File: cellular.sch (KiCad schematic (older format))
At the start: 16 parts

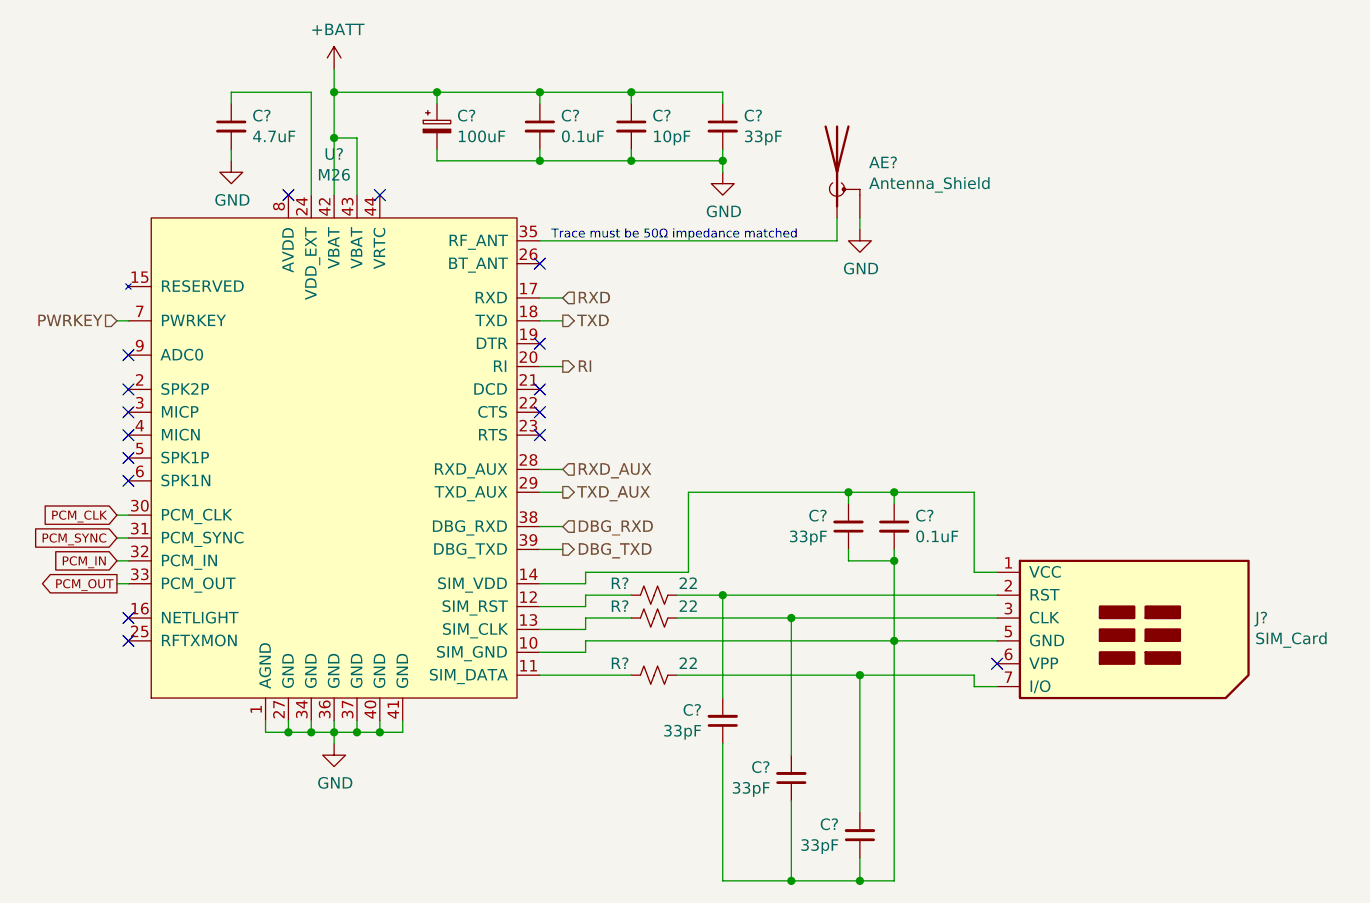
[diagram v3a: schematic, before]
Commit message: annotate schematic and tweak some footprint associations
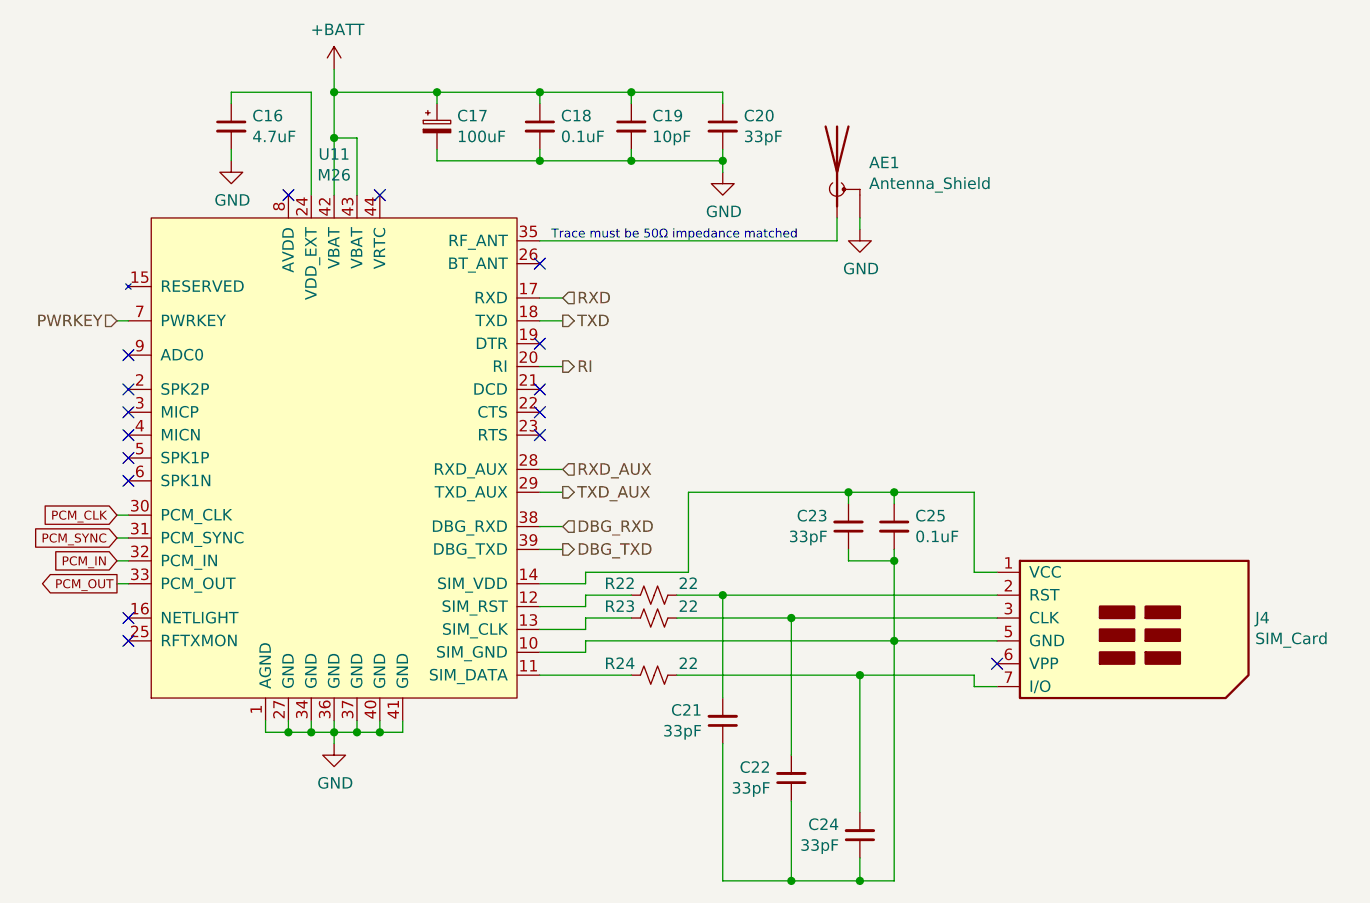
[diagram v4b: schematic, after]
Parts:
- gave numbers to parts that had none: 16
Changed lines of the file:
@@
 $EndDescr
 $Comp
-L phone:M26 U?
+L phone:M26 U11
 U 1 1 5C9AECA6
 P 2250 2550
-F 0 "U?" H 2250 3878 50  0000 C CNN
+F 0 "U11" H 2250 3878 50  0000 C CNN
 F 1 "M26" H 2250 3787 50  0000 C CNN
 F 2 "phone:M26" H 2250 2550 50  0001 C CNN
@@
 NoConn ~ 1350 2650
 $Comp
-L Device:Antenna_Shield AE?
+L Device:Antenna_Shield AE1
 U 1 1 5C9AEE16
 P 4450 1300
-F 0 "AE?" H 4590 1341 50  0000 L CNN
+F 0 "AE1" H 4590 1341 50  0000 L CNN
 F 1 "Antenna_Shield" H 4590 1250 50  0000 L CNN
 F 2 "Connector_Coaxial:U.FL_Molex_MCRF_73412-0110_Vertical" H 4450 1400 50  0001 C CNN
@@
 	4450 1600 4450 1500
 $Comp
-L power:GND #PWR?
+L power:GND #PWR058
 U 1 1 5C9AEED4
 P 4550 1550
-F 0 "#PWR?" H 4550 1300 50  0001 C CNN
+F 0 "#PWR058" H 4550 1300 50  0001 C CNN
 F 1 "GND" H 4555 1377 50  0000 C CNN
 F 2 "" H 4550 1550 50  0001 C CNN
@@
 NoConn ~ 1350 3250
 $Comp
-L power:GND #PWR?
+L power:GND #PWR056
 U 1 1 5C9B042C
 P 2250 3800
-F 0 "#PWR?" H 2250 3550 50  0001 C CNN
+F 0 "#PWR056" H 2250 3550 50  0001 C CNN
 F 1 "GND" H 2255 3627 50  0000 C CNN
 F 2 "" H 2250 3800 50  0001 C CNN
@@
 	2250 3750 2250 3800
 $Comp
-L Connector:SIM_Card J?
+L Connector:SIM_Card J4
 U 1 1 5C9B0C92
 P 5650 3350
-F 0 "J?" H 6279 3450 50  0000 L CNN
+F 0 "J4" H 6279 3450 50  0000 L CNN
 F 1 "SIM_Card" H 6279 3359 50  0000 L CNN
 F 2 "phone:7112S0815X19LF" H 5650 3700 50  0001 C CNN
@@
 	2350 1150 2250 1150
 $Comp
-L power:+BATT #PWR?
+L power:+BATT #PWR055
 U 1 1 5CA67C60
 P 2250 850
-F 0 "#PWR?" H 2250 700 50  0001 C CNN
+F 0 "#PWR055" H 2250 700 50  0001 C CNN
 F 1 "+BATT" H 2265 1023 50  0000 C CNN
 F 2 "" H 2250 850 50  0001 C CNN
@@
 NoConn ~ 2050 1400
 $Comp
-L Device:C_Small C?
+L Device:C_Small C16
 U 1 1 5D5D7303
 P 1800 1100
-F 0 "C?" H 1892 1146 50  0000 L CNN
+F 0 "C16" H 1892 1146 50  0000 L CNN
 F 1 "4.7uF" H 1892 1055 50  0000 L CNN
 F 2 "Capacitor_SMD:C_0603_1608Metric_Pad1.05x0.95mm_HandSolder" H 1800 1100 50  0001 C CNN
@@
 $EndComp
 $Comp
-L power:GND #PWR?
+L power:GND #PWR054
 U 1 1 5D5D9D65
 P 1800 1250
-F 0 "#PWR?" H 1800 1000 50  0001 C CNN
+F 0 "#PWR054" H 1800 1000 50  0001 C CNN
 F 1 "GND" H 1805 1077 50  0000 C CNN
 F 2 "" H 1800 1250 50  0001 C CNN
@@
 	1800 950  1800 1000
 $Comp
-L Device:C_Small C?
+L Device:C_Small C25
 U 1 1 5D5DD206
 P 4700 2850
-F 0 "C?" H 4792 2896 50  0000 L CNN
+F 0 "C25" H 4792 2896 50  0000 L CNN
 F 1 "0.1uF" H 4792 2805 50  0000 L CNN
 F 2 "Capacitor_SMD:C_0603_1608Metric_Pad1.05x0.95mm_HandSolder" H 4700 2850 50  0001 C CNN
@@
 NoConn ~ 5150 3450
 $Comp
-L Device:R_Small_US R?
+L Device:R_Small_US R22
 U 1 1 5D5E2ECB
 P 3650 3150
-F 0 "R?" V 3600 3000 50  0000 C CNN
+F 0 "R22" V 3600 3000 50  0000 C CNN
 F 1 "22" V 3600 3300 50  0000 C CNN
 F 2 "Resistor_SMD:R_0603_1608Metric_Pad1.05x0.95mm_HandSolder" H 3650 3150 50  0001 C CNN
@@
 	3750 3150 3950 3150
 $Comp
-L Device:R_Small_US R?
+L Device:R_Small_US R23
 U 1 1 5D5E8317
 P 3650 3250
-F 0 "R?" V 3600 3100 50  0000 C CNN
+F 0 "R23" V 3600 3100 50  0000 C CNN
 F 1 "22" V 3600 3400 50  0000 C CNN
 F 2 "Resistor_SMD:R_0603_1608Metric_Pad1.05x0.95mm_HandSolder" H 3650 3250 50  0001 C CNN
@@
 Connection ~ 4700 2700
 $Comp
-L Device:R_Small_US R?
+L Device:R_Small_US R24
 U 1 1 5D5F3F1B
 P 3650 3500
-F 0 "R?" V 3600 3350 50  0000 C CNN
+F 0 "R24" V 3600 3350 50  0000 C CNN
 F 1 "22" V 3600 3650 50  0000 C CNN
 F 2 "Resistor_SMD:R_0603_1608Metric_Pad1.05x0.95mm_HandSolder" H 3650 3500 50  0001 C CNN
@@
 	5050 3500 4550 3500
 $Comp
-L Device:C_Small C?
+L Device:C_Small C23
 U 1 1 5D5F7DFB
 P 4500 2850
-F 0 "C?" H 4409 2804 50  0000 R CNN
+F 0 "C23" H 4409 2804 50  0000 R CNN
 F 1 "33pF" H 4409 2895 50  0000 R CNN
 F 2 "Capacitor_SMD:C_0603_1608Metric_Pad1.05x0.95mm_HandSolder" H 4500 2850 50  0001 C CNN
@@
 	4500 2700 4700 2700
 $Comp
-L Device:C_Small C?
+L Device:C_Small C21
 U 1 1 5D5FC3FC
 P 3950 3700
-F 0 "C?" H 3859 3654 50  0000 R CNN
+F 0 "C21" H 3859 3654 50  0000 R CNN
 F 1 "33pF" H 3859 3745 50  0000 R CNN
 F 2 "Capacitor_SMD:C_0603_1608Metric_Pad1.05x0.95mm_HandSolder" H 3950 3700 50  0001 C CNN
@@
 	3950 3150 5150 3150
 $Comp
-L Device:C_Small C?
+L Device:C_Small C22
 U 1 1 5D5FDAEC
 P 4250 3950
-F 0 "C?" H 4159 3904 50  0000 R CNN
+F 0 "C22" H 4159 3904 50  0000 R CNN
 F 1 "33pF" H 4159 3995 50  0000 R CNN
 F 2 "Capacitor_SMD:C_0603_1608Metric_Pad1.05x0.95mm_HandSolder" H 4250 3950 50  0001 C CNN
@@
 	3150 3500 3550 3500
 $Comp
-L Device:C_Small C?
+L Device:C_Small C24
 U 1 1 5D60FB3C
 P 4550 4200
-F 0 "C?" H 4459 4154 50  0000 R CNN
+F 0 "C24" H 4459 4154 50  0000 R CNN
 F 1 "33pF" H 4459 4245 50  0000 R CNN
 F 2 "Capacitor_SMD:C_0603_1608Metric_Pad1.05x0.95mm_HandSolder" H 4550 4200 50  0001 C CNN
@@
 Connection ~ 4250 4400
 $Comp
-L Device:CP_Small C?
+L Device:CP_Small C17
 U 1 1 5D622E7F
 P 2700 1100
-F 0 "C?" H 2788 1146 50  0000 L CNN
+F 0 "C17" H 2788 1146 50  0000 L CNN
 F 1 "100uF" H 2788 1055 50  0000 L CNN
 F 2 "Capacitor_Tantalum_SMD:CP_EIA-3528-15_AVX-H_Pad1.50x2.35mm_HandSolder" H 2700 1100 50  0001 C CNN
@@
 $EndComp
 $Comp
-L Device:C_Small C?
+L Device:C_Small C18
 U 1 1 5D623741
 P 3150 1100
-F 0 "C?" H 3242 1146 50  0000 L CNN
+F 0 "C18" H 3242 1146 50  0000 L CNN
 F 1 "0.1uF" H 3242 1055 50  0000 L CNN
 F 2 "Capacitor_SMD:C_0603_1608Metric_Pad1.05x0.95mm_HandSolder" H 3150 1100 50  0001 C CNN
@@
 $EndComp
 $Comp
-L Device:C_Small C?
+L Device:C_Small C19
 U 1 1 5D626C11
 P 3550 1100
-F 0 "C?" H 3642 1146 50  0000 L CNN
+F 0 "C19" H 3642 1146 50  0000 L CNN
 F 1 "10pF" H 3642 1055 50  0000 L CNN
 F 2 "Capacitor_SMD:C_0603_1608Metric_Pad1.05x0.95mm_HandSolder" H 3550 1100 50  0001 C CNN
@@
 $EndComp
 $Comp
-L Device:C_Small C?
+L Device:C_Small C20
 U 1 1 5D627055
 P 3950 1100
-F 0 "C?" H 4042 1146 50  0000 L CNN
+F 0 "C20" H 4042 1146 50  0000 L CNN
 F 1 "33pF" H 4042 1055 50  0000 L CNN
 F 2 "Capacitor_SMD:C_0603_1608Metric_Pad1.05x0.95mm_HandSolder" H 3950 1100 50  0001 C CNN
@@
 	3550 1250 3150 1250
 $Comp
-L power:GND #PWR?
+L power:GND #PWR057
 U 1 1 5D634214
 P 3950 1300
-F 0 "#PWR?" H 3950 1050 50  0001 C CNN
+F 0 "#PWR057" H 3950 1050 50  0001 C CNN
 F 1 "GND" H 3955 1127 50  0000 C CNN
 F 2 "" H 3950 1300 50  0001 C CNN
